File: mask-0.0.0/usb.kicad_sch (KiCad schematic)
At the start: 13 parts, among them J1 USB_C_Receptacle_USB2.0, J2 USB_C_Receptacle_USB2.0

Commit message: udpate routing
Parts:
- renumbered C1 to C5, C2 to C6, C3 to C7, C4 to C8, D36 to D42, J1 to J3, J2 to J4, R1 to R4, R2 to R5, R3 to R6
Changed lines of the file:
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@@
   (symbol (lib_id "power:+5V") (at 191.77 107.315 0) (unit 1)
     (in_bom yes) (on_board yes)
-    (property "Reference" "#PWR0101" (id 0) (at 191.77 111.125 0)
+    (property "Reference" "#PWR028" (id 0) (at 191.77 111.125 0)
       (effects (font (size 1.27 1.27)) hide)
     )
@@
   (symbol (lib_id "power:GND") (at 156.21 125.095 0) (unit 1)
     (in_bom yes) (on_board yes) (fields_autoplaced)
-    (property "Reference" "#PWR0103" (id 0) (at 156.21 131.445 0)
+    (property "Reference" "#PWR027" (id 0) (at 156.21 131.445 0)
       (effects (font (size 1.27 1.27)) hide)
     )
@@
   (symbol (lib_id "power:GND") (at 191.77 125.095 0) (unit 1)
     (in_bom yes) (on_board yes) (fields_autoplaced)
-    (property "Reference" "#PWR0102" (id 0) (at 191.77 131.445 0)
+    (property "Reference" "#PWR029" (id 0) (at 191.77 131.445 0)
       (effects (font (size 1.27 1.27)) hide)
     )
@@
   (symbol (lib_id "Device:R") (at 97.79 59.055 0) (unit 1)
     (in_bom yes) (on_board yes) (fields_autoplaced)
-    (property "Reference" "R1" (id 0) (at 99.5681 58.1465 0)
+    (property "Reference" "R4" (id 0) (at 99.5681 58.1465 0)
       (effects (font (size 1.27 1.27)) (justify left))
     )
@@
   (symbol (lib_id "Device:R") (at 106.68 59.055 0) (unit 1)
     (in_bom yes) (on_board yes) (fields_autoplaced)
-    (property "Reference" "R2" (id 0) (at 108.4581 58.1465 0)
+    (property "Reference" "R5" (id 0) (at 108.4581 58.1465 0)
       (effects (font (size 1.27 1.27)) (justify left))
     )
@@
   (symbol (lib_id "Device:R") (at 140.97 116.205 0) (unit 1)
     (in_bom yes) (on_board yes) (fields_autoplaced)
-    (property "Reference" "R3" (id 0) (at 142.7481 115.2965 0)
+    (property "Reference" "R6" (id 0) (at 142.7481 115.2965 0)
       (effects (font (size 1.27 1.27)) (justify left))
     )
@@
   (symbol (lib_id "Device:C") (at 127 116.205 0) (unit 1)
     (in_bom yes) (on_board yes) (fields_autoplaced)
-    (property "Reference" "C1" (id 0) (at 129.9211 115.2965 0)
+    (property "Reference" "C5" (id 0) (at 129.9211 115.2965 0)
       (effects (font (size 1.27 1.27)) (justify left))
     )
@@
   (symbol (lib_id "Device:C") (at 163.83 116.205 0) (unit 1)
     (in_bom yes) (on_board yes) (fields_autoplaced)
-    (property "Reference" "C2" (id 0) (at 166.7511 115.2965 0)
+    (property "Reference" "C6" (id 0) (at 166.7511 115.2965 0)
       (effects (font (size 1.27 1.27)) (justify left))
     )
@@
   (symbol (lib_id "Device:C") (at 181.61 116.205 0) (unit 1)
     (in_bom yes) (on_board yes) (fields_autoplaced)
-    (property "Reference" "C3" (id 0) (at 184.5311 115.2965 0)
+    (property "Reference" "C7" (id 0) (at 184.5311 115.2965 0)
       (effects (font (size 1.27 1.27)) (justify left))
     )
@@
   (symbol (lib_id "Device:C") (at 191.77 116.205 0) (unit 1)
     (in_bom yes) (on_board yes) (fields_autoplaced)
-    (property "Reference" "C4" (id 0) (at 194.6911 115.2965 0)
+    (property "Reference" "C8" (id 0) (at 194.6911 115.2965 0)
       (effects (font (size 1.27 1.27)) (justify left))
     )
@@
   (symbol (lib_id "Power_Protection:PRTR5V0U2X") (at 127 84.455 0) (unit 1)
     (in_bom yes) (on_board yes)
-    (property "Reference" "D36" (id 0) (at 140.3351 83.5465 0)
+    (property "Reference" "D42" (id 0) (at 140.3351 83.5465 0)
       (effects (font (size 1.27 1.27)) (justify left))
     )
@@
   (symbol (lib_id "Connector:USB_C_Receptacle_USB2.0") (at 68.58 59.055 0) (unit 1)
     (in_bom yes) (on_board yes) (fields_autoplaced)
-    (property "Reference" "J1" (id 0) (at 71.0565 37.3084 0))
+    (property "Reference" "J3" (id 0) (at 71.0565 37.3084 0))
     (property "Value" "USB_C_Receptacle_USB2.0" (id 1) (at 71.0565 40.0835 0))
     (property "Footprint" "Connector_USB:USB_C_Receptacle_JAE_DX07S016JA1R1500" (id 2) (at 72.39 59.055 0)
@@
   (symbol (lib_id "Connector:USB_C_Receptacle_USB2.0") (at 69.85 133.985 0) (unit 1)
     (in_bom yes) (on_board yes) (fields_autoplaced)
-    (property "Reference" "J2" (id 0) (at 72.3265 112.2384 0))
+    (property "Reference" "J4" (id 0) (at 72.3265 112.2384 0))
     (property "Value" "USB_C_Receptacle_USB2.0" (id 1) (at 72.3265 115.0135 0))
     (property "Footprint" "Connector_USB:USB_C_Receptacle_JAE_DX07S016JA1R1500" (id 2) (at 73.66 133.985 0)

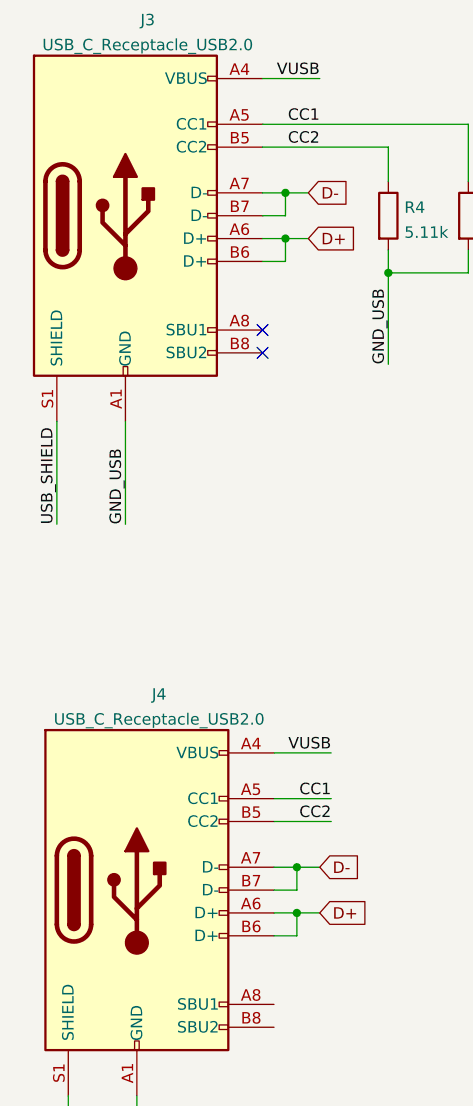
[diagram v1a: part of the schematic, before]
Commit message: mask-0.0.0: begin of matrix routing
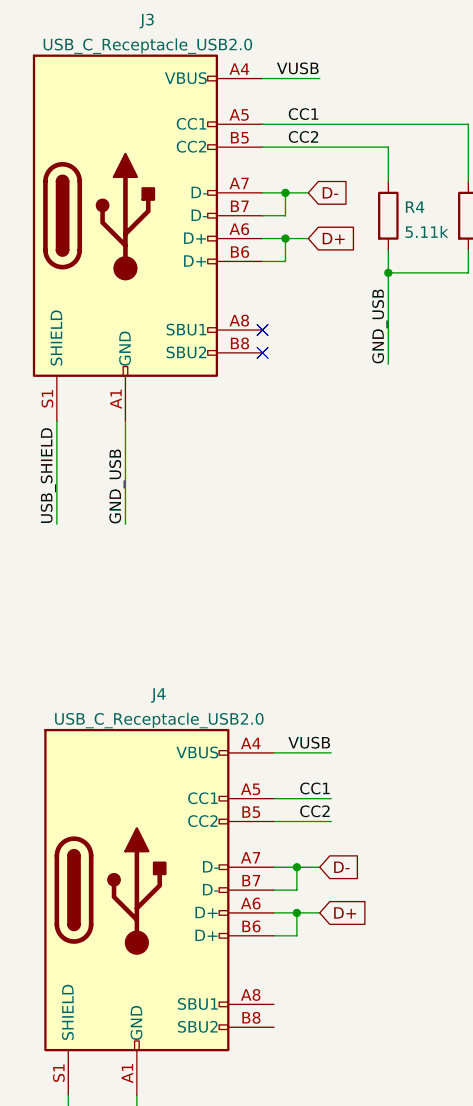
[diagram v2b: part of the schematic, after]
